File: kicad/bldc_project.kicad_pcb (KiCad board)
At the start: 4 copper layers, 100 x 60 mm, 158 parts, among them J1 Conn_ARM_SWD_TagConnect_TC203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, J2 Screw_Terminal_01x03, J3 Screw_Terminal_01x03, J4 TYPE-C-31-M-12, Q1 IRFZ44NPBF, Q2 IRFZ44NPBF, Q3 IRFZ44NPBF, Q4 IRFZ44NPBF, Q5 IRFZ44NPBF, Q6 IRFZ44NPBF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

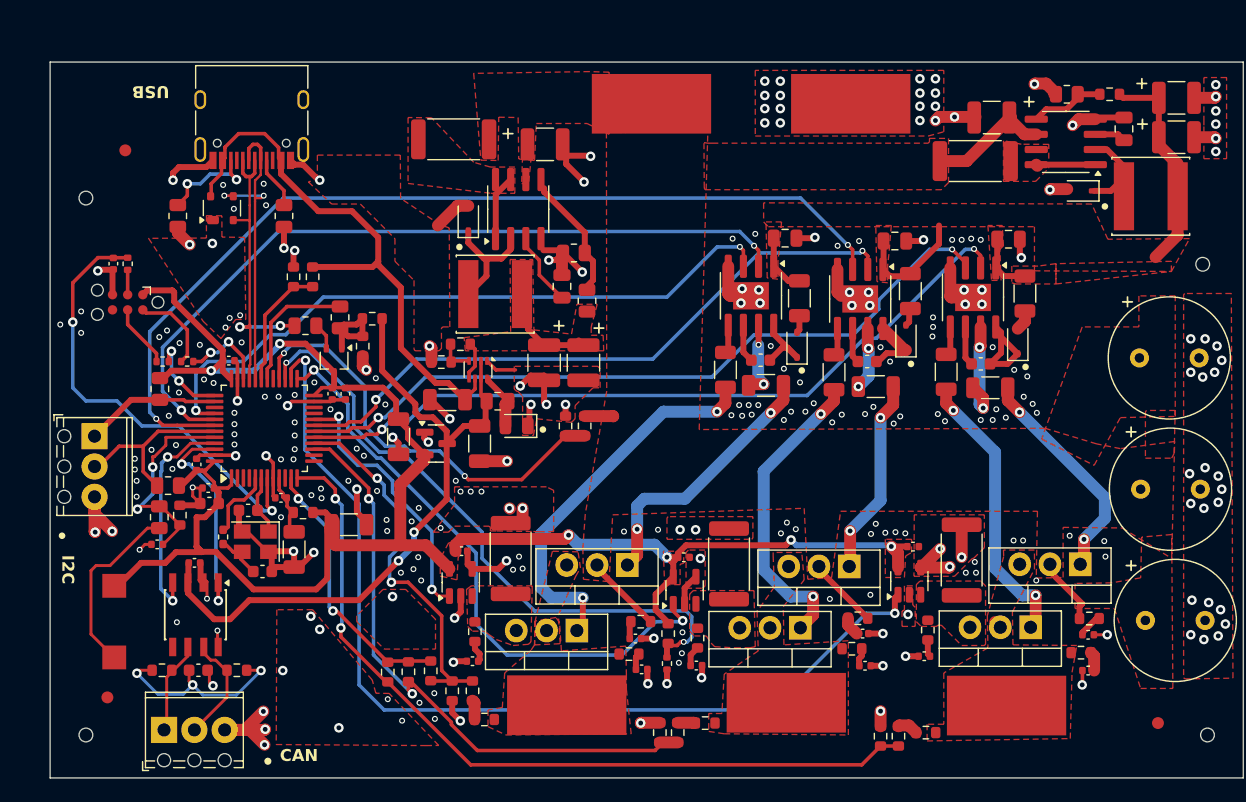
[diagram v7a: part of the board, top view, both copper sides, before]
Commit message: [kicad] Added testpoints, added 1 amp fuses at 2 buck converters
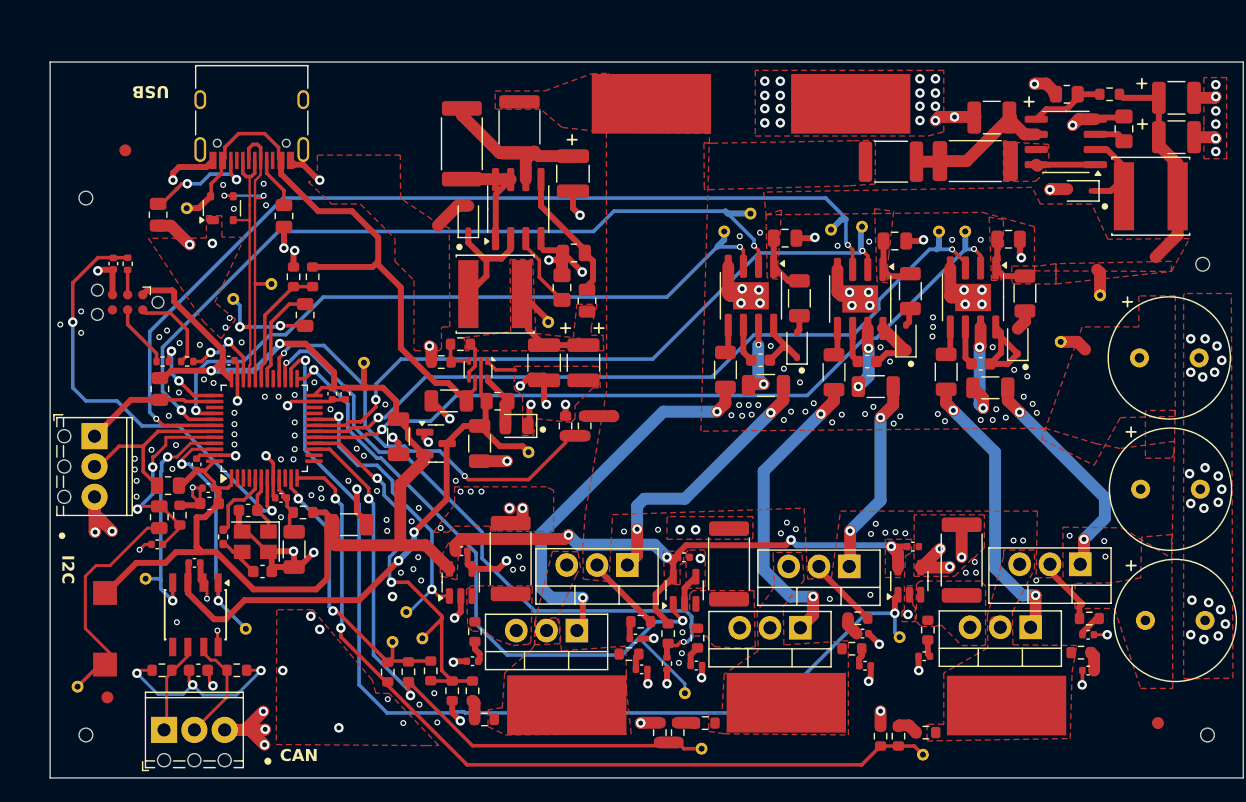
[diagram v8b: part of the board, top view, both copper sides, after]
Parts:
- removed Q7: BC847BW,115, Package_TO_SOT_SMD:SOT-323_SC-70
- removed R51: 1.5k, Resistor_SMD:R_0805_2012Metric
- removed R52: 12k, Resistor_SMD:R_0603_1608Metric
- removed R53: 33k, Resistor_SMD:R_0603_1608Metric
- added F1: Polyfuse_Small, Fuse:Fuse_1812_4532Metric, F.Cu at (80.5, 86.0)
- added F2: Polyfuse_Small, Fuse:Fuse_1812_4532Metric, F.Cu at (111.7, 88.8)
- added TP1: TestPoint_Probe, TestPoint:TestPoint_THTPad_D1.0mm_Drill0.5mm, B.Cu at (67.5, 105.7)
- added TP10: TestPoint_Probe, TestPoint:TestPoint_THTPad_D1.0mm_Drill0.5mm, B.Cu at (99.9, 93.2)
- added TP11: TestPoint_Probe, TestPoint:TestPoint_THTPad_D1.0mm_Drill0.5mm, B.Cu at (115.7, 94.7)
- added TP12: TestPoint_Probe, TestPoint:TestPoint_THTPad_D1.0mm_Drill0.5mm, B.Cu at (106.7, 94.5)
- added TP13: TestPoint_Probe, TestPoint:TestPoint_THTPad_D1.0mm_Drill0.5mm, B.Cu at (97.7, 94.7)
- added TP14: TestPoint_Probe, TestPoint:TestPoint_THTPad_D1.0mm_Drill0.5mm, B.Cu at (112.4, 128.7)
- added TP15: TestPoint_Probe, TestPoint:TestPoint_THTPad_D1.0mm_Drill0.5mm, B.Cu at (94.4, 133.4)
- added TP16: TestPoint_Probe, TestPoint:TestPoint_THTPad_D1.0mm_Drill0.5mm, B.Cu at (71.0, 126.6)
- added TP17: TestPoint_Probe, TestPoint:TestPoint_THTPad_D1.0mm_Drill0.5mm, B.Cu at (114.3, 138.6)
- added TP18: TestPoint_Probe, TestPoint:TestPoint_THTPad_D1.0mm_Drill0.5mm, B.Cu at (56.5, 100.3)
- added TP19: TestPoint_Probe, TestPoint:TestPoint_THTPad_D1.0mm_Drill0.5mm, B.Cu at (59.8, 99.1)
- added TP2: TestPoint_Probe, TestPoint:TestPoint_THTPad_D1.0mm_Drill0.5mm, B.Cu at (83.0, 102.3)
- added TP20: TestPoint_Probe, TestPoint:TestPoint_THTPad_D1.0mm_Drill0.5mm, B.Cu at (52.6, 92.8)
- added TP21: TestPoint_Probe, TestPoint:TestPoint_THTPad_D1.0mm_Drill0.5mm, B.Cu at (43.5, 132.8)
- added TP22: TestPoint_Probe, TestPoint:TestPoint_THTPad_D1.0mm_Drill0.5mm, B.Cu at (95.8, 138.1)
- added TP23: TestPoint_Probe, TestPoint:TestPoint_THTPad_D1.0mm_Drill0.5mm, B.Cu at (72.4, 128.8)
- added TP24: TestPoint_Probe, TestPoint:TestPoint_THTPad_D1.0mm_Drill0.5mm, B.Cu at (69.9, 129.1)
- added TP3: TestPoint_Probe, TestPoint:TestPoint_THTPad_D1.0mm_Drill0.5mm, B.Cu at (81.3, 113.2)
- added TP4: TestPoint_Probe, TestPoint:TestPoint_THTPad_D1.0mm_Drill0.5mm, B.Cu at (129.2, 100.0)
- added TP5: TestPoint_Probe, TestPoint:TestPoint_THTPad_D1.0mm_Drill0.5mm, B.Cu at (125.9, 104.0)
- added TP6: TestPoint_Probe, TestPoint:TestPoint_THTPad_D1.0mm_Drill0.5mm, B.Cu at (49.2, 123.8)
- added TP7: TestPoint_Probe, TestPoint:TestPoint_THTPad_D1.0mm_Drill0.5mm, B.Cu at (57.6, 128.0)
- added TP8: TestPoint_Probe, TestPoint:TestPoint_THTPad_D1.0mm_Drill0.5mm, B.Cu at (117.9, 94.7)
- added TP9: TestPoint_Probe, TestPoint:TestPoint_THTPad_D1.0mm_Drill0.5mm, B.Cu at (109.2, 94.3)
- C42, C43: footprint Capacitor_SMD:C_0805_2012Metric -> Capacitor_SMD:C_0805_2012Metric_Pad1.18x1.45mm_HandSolder
- R34: value 200k -> 330k
- moved C44 3.39 mm to (85.0, 89.9), turned to -90 degrees
- moved R56 1.65 mm to (50.2, 93.3)
- moved SW1 0.98 mm to (45.8, 128.0)
- moved R57 0.90 mm to (62.6, 101.7), turned to 90 degrees
- moved R59 0.78 mm to (75.7, 87.3), turned to -90 degrees
- moved C38 0.16 mm to (74.6, 108.9)
- moved C42 0.10 mm to (84.1, 99.4)
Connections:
- net Net-(R36-Pad1) renamed /CPU/BOOT0_R
- C44 pad 1: +BATT -> Net-(U10-Vin)
- C45 pad 1: +BATT -> Net-(U11-Vin)
- R57 pad 2: Net-(Q7-E) -> USB_RENUMn
- R59 pad 1: +BATT -> Net-(U10-Vin)
- R60 pad 1: +BATT -> Net-(U11-Vin)
- U10 pad 6: +BATT -> Net-(U10-Vin)
- U11 pad 6: +BATT -> Net-(U11-Vin)
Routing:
- net Net-(U10-Vin): track 0.00 -> 12.7 mm
- net Net-(U11-Vin): track 0.00 -> 12.4 mm
- net +5V: track 57.6 -> 49.3 mm
- net +BATT: track 31.4 -> 23.4 mm
- net Net-(Q7-B): track 7.62 -> 0.00 mm
- net PhaseV_CURRENT: track 50.2 -> 56.3 mm
- net /POWER/VBUCK5_IN: track 5.48 -> 10.1 mm
- net PhaseW_SWITCH: track 65.1 -> 69.0 mm
- net USB_DP: track 27.3 -> 30.9 mm
- net /CPU/BOOT0_R: track 15.3 -> 18.7 mm
- net /CPU/CAN_TX: track 18.5 -> 21.8 mm
- net /POWER/VBUCK5_OUT: track 11.9 -> 15.2 mm
- net +10V: track 38.4 -> 35.3 mm
- net PhaseW_CURRENT: track 22.6 -> 25.5 mm
- net PhaseV_SWITCH: track 54.1 -> 57.0 mm
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- removed copper zone on F.Cu, net /POWER/VBUCK5_IN
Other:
- board text added: "3.3V"
- board text added: "BUCK5_O"
- board text added: "CAN_RX"
- board text added: "CAN_TX"
- board text added: "D+"
- board text added: "D-"
- board text added: "G_V"
- board text added: "U_I"
- board text added: "U_SD"
- board text added: "U_SW"
- board text added: "V_I"
- board text added: "V_SD"
- board text added: "V_SW"
- board text added: "V_U"
- board text added: "V_USB"
- board text added: "V_V"
- board text added: "W_I"
- board text added: "W_SD"
- board text added: "W_SW"
- board text added: "W_V"
- board text removed: "GND"
- board text removed: "PhaseU"
- board text removed: "PhaseV"
- board text removed: "PhaseW"
